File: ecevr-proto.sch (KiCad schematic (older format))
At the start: 30 parts, among them SW1 SW_Push

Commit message: WIP: (save)
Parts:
- removed BT1: CR1220, Battery:BatteryHolder_Keystone_500, symbol Device:Battery_Cell
- removed D1, D2, D3, D4, D5, D6, D7, D8: LED, LED_SMD:LED_0603_1608Metric, symbol Device:LED
- removed H1, H2, H3, H4: MountingHole_Pad, MountingHole:MountingHole_3.2mm_M3_ISO14580_Pad_TopBottom, symbol Mechanical:MountingHole_Pad
- removed JP1: TEST, Connector_PinHeader_2.54mm:PinHeader_1x02_P2.54mm_Vertical, symbol Device:Jumper_NO_Small
- removed JP2: Jumper, Connector_PinHeader_2.54mm:PinHeader_1x02_P2.54mm_Vertical, symbol Device:Jumper
- removed R1, R2: 10k, Resistor_SMD:R_0603_1608Metric, symbol trigbox:R10k
- removed R10, R3, R4, R5, R6, R7, R8, R9: 1k, Resistor_SMD:R_0603_1608Metric, symbol Device:R_Small
- removed SW1: SW_Push, Button_Switch_SMD:SW_SPST_PTS810, symbol Switch:SW_Push
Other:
- note removed: "Boot Mode:\nOff -> SPI\nOn -> SDCARD"
- note removed: "GREEN LED"
- note removed: "Mounting holes\nfor mezzanine"
- note removed: "RED LED"
- note removed: "RESET"

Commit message: WIP: point before we change to OSH/relaxed process
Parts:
- added U14: 74LVC1G06, proj_footprints:SOT-5x3, symbol fmc:74LVC1G06
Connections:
- net +3V3: now also U14.5 (VCC)
- net GND: now also U14.3 (GND)
- new net IO_L5P_T0_AD9P_15: U14.2
- new net SFP Connector/TX_DISABLE: U14.4
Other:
- moved on the sheet: H5, H6, H7, H8

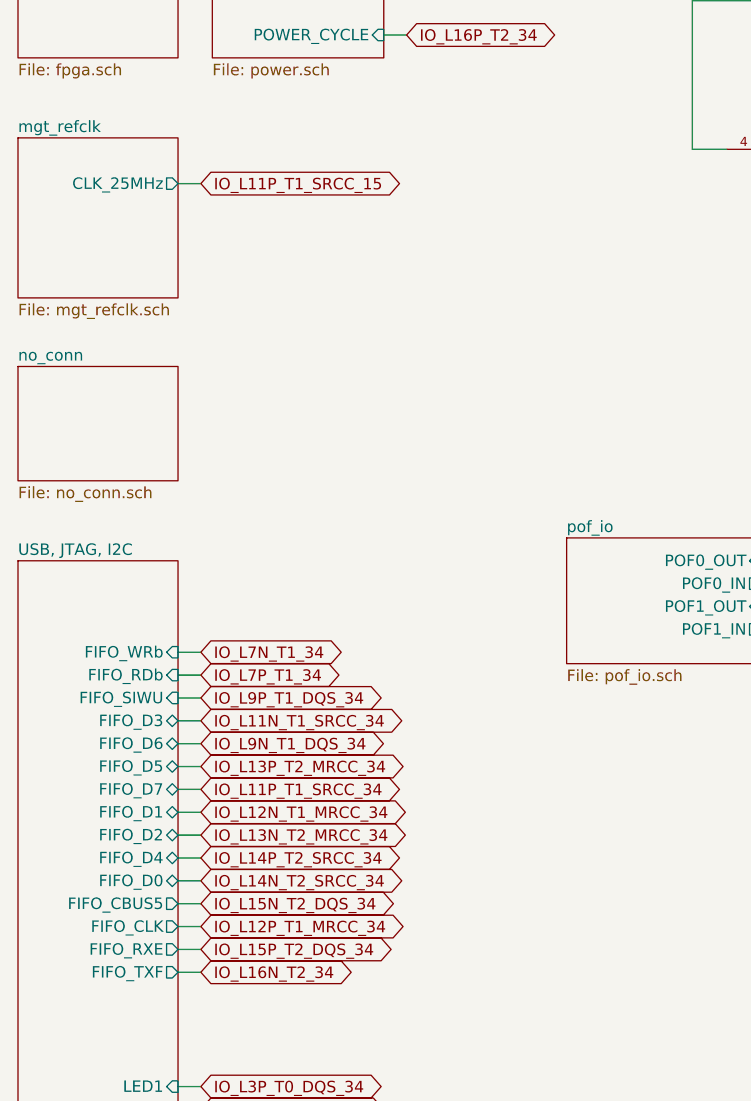
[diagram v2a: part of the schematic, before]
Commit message: re-routed with more relaxed specs (that eurocircuits can also meet)
No chance with OSH, however...

Going to place stuff on the board now...
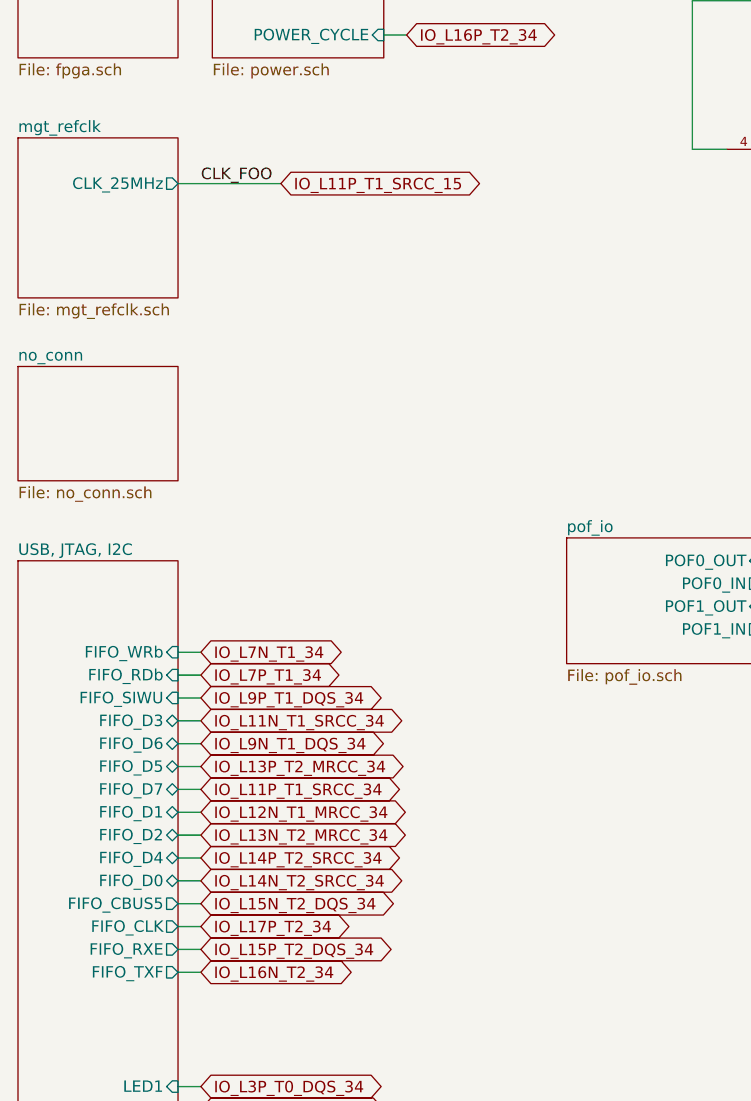
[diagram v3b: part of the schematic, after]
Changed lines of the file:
@@
 Wire Wire Line
 	7750 5200 7900 5200
-Text GLabel 1700 2050 2    50   BiDi ~ 0
+Text GLabel 2050 2050 2    50   BiDi ~ 0
 IO_L11P_T1_SRCC_15
 Text GLabel 7700 6050 0    50   BiDi ~ 0
@@
 Text GLabel 1700 4800 2    50   BiDi ~ 0
 IO_L12N_T1_MRCC_34
-Text GLabel 1700 5300 2    50   BiDi ~ 0
-IO_L12P_T1_MRCC_34
 Text GLabel 1700 4900 2    50   BiDi ~ 0
 IO_L13N_T2_MRCC_34
@@
 IO_25_14
 Wire Wire Line
-	1600 2050 1700 2050
+	1600 2050 2050 2050
 Wire Wire Line
 	1600 1050 1750 1050
@@
 Wire Wire Line
 	4150 4000 4250 4000
+Text GLabel 1700 5300 2    50   BiDi ~ 0
+IO_L17P_T2_34
+Text Label 1700 2050 0    50   ~ 0
+CLK_FOO
 $EndSCHEMATC

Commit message: further work...
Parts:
- H5, H6, H7, H8: Manufacturer (none) -> Essentra; Part (none) -> FF-13-P3.5X6.0B
- U21: renamed from U14; footprint proj_footprints:SOT-5x3 -> Package_TO_SOT_SMD:SOT-353_SC-70-5; symbol fmc:74LVC1G06 -> fmc:74LVC1G38
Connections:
- net +1V8: now also U21.5 (VCC)
- net +3V3: no longer U21.5 (VCC)
- net IO_L5P_T0_AD9P_15: no longer U21.2
- net IO_L3N_T0_DQS_AD1N_15: now reaches U21.1
- net IO_L3N_T0_DQS_AD1N_15: now also U21.2

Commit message: added 3rd GPIO
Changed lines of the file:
@@
 $Descr USLetter 11000 8500
 encoding utf-8
-Sheet 1 20
+Sheet 1 21
 Title ""
 Date ""
@@
 F63 "TMS" I L 7900 6150 50
 F64 "JTAG_EN" O L 7900 6450 50
+F65 "FPGA_IO3_DIR" I R 9150 5300 50
+F66 "FPGA_IO3_DAT" B R 9150 5200 50
 $EndSheet
 Text GLabel 9300 5850 2    50   BiDi ~ 0
@@
 Wire Wire Line
 	1700 7400 1700 7450
+Text GLabel 9300 5200 2    50   BiDi ~ 0
+IO_L17P_T2_A14_D30_14
+Wire Wire Line
+	9300 5200 9150 5200
+Text GLabel 9300 5300 2    50   BiDi ~ 0
+IO_L20N_T3_A07_D23_14
+Wire Wire Line
+	9300 5300 9150 5300
 $EndSCHEMATC
